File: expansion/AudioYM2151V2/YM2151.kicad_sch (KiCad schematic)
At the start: 17 parts, among them U3 LTC6903, U4 YM2151, U5 YM3012, U6 TL064

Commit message: more work on new audio card
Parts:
- added C48, C49: 4.7uF, symbol Device:C_Polarized
- added R13, R14: 3K9, symbol Device:R
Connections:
- net YM_AUDIO_L: now also R13.2; no longer U6.1, U6.2 (-)
- net YM_AUDIO_R: now also R14.2; no longer U6.6 (-), U6.7
- new net: C48.1, U6.1, U6.2 (-)
- new net: C49.1, U6.6 (-), U6.7
- new net: C49.2, R14.1
- new net: C48.2, R13.1
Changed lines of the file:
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@@
   (junction (at 83.82 68.58) (diameter 0) (color 0 0 0 0)
   )
+  (junction (at 92.71 179.07) (diameter 0) (color 0 0 0 0)
+  )
+  (junction (at 246.38 127) (diameter 0) (color 0 0 0 0)
+  )
+  (junction (at 92.71 166.37) (diameter 0) (color 0 0 0 0)
+  )
+  (junction (at 135.89 179.07) (diameter 0) (color 0 0 0 0)
+  )
+  (junction (at 246.38 144.78) (diameter 0) (color 0 0 0 0)
+  )
+  (junction (at 90.17 123.19) (diameter 0) (color 0 0 0 0)
+  )
+  (junction (at 124.46 119.38) (diameter 0) (color 0 0 0 0)
+  )
+  (junction (at 121.92 113.03) (diameter 0) (color 0 0 0 0)
+  )
+  (junction (at 207.01 31.75) (diameter 0) (color 0 0 0 0)
+  )
+  (junction (at 170.18 143.51) (diameter 0) (color 0 0 0 0)
+  )
+  (junction (at 179.07 41.91) (diameter 0) (color 0 0 0 0)
+  )
+  (junction (at 135.89 166.37) (diameter 0) (color 0 0 0 0)
+  )
+  (junction (at 127 121.92) (diameter 0) (color 0 0 0 0)
+  )
+  (junction (at 204.47 115.57) (diameter 0) (color 0 0 0 0)
+  )
+  (junction (at 207.01 64.77) (diameter 0) (color 0 0 0 0)
+  )
+  (junction (at 156.21 44.45) (diameter 0) (color 0 0 0 0)
+  )
+  (junction (at 146.05 39.37) (diameter 0) (color 0 0 0 0)
+  )
+  (junction (at 232.41 34.29) (diameter 0) (color 0 0 0 0)
+  )
+  (junction (at 129.54 107.95) (diameter 0) (color 0 0 0 0)
+  )
+  (junction (at 69.85 147.32) (diameter 0) (color 0 0 0 0)
+  )
   (junction (at 232.41 67.31) (diameter 0) (color 0 0 0 0)
-  )
-  (junction (at 92.71 179.07) (diameter 0) (color 0 0 0 0)
-  )
-  (junction (at 232.41 34.29) (diameter 0) (color 0 0 0 0)
-  )
-  (junction (at 246.38 127) (diameter 0) (color 0 0 0 0)
-  )
-  (junction (at 92.71 166.37) (diameter 0) (color 0 0 0 0)
-  )
-  (junction (at 135.89 179.07) (diameter 0) (color 0 0 0 0)
-  )
-  (junction (at 246.38 144.78) (diameter 0) (color 0 0 0 0)
-  )
-  (junction (at 90.17 123.19) (diameter 0) (color 0 0 0 0)
-  )
-  (junction (at 124.46 119.38) (diameter 0) (color 0 0 0 0)
-  )
-  (junction (at 121.92 113.03) (diameter 0) (color 0 0 0 0)
-  )
-  (junction (at 207.01 31.75) (diameter 0) (color 0 0 0 0)
-  )
-  (junction (at 170.18 143.51) (diameter 0) (color 0 0 0 0)
-  )
-  (junction (at 179.07 41.91) (diameter 0) (color 0 0 0 0)
-  )
-  (junction (at 135.89 166.37) (diameter 0) (color 0 0 0 0)
-  )
-  (junction (at 127 121.92) (diameter 0) (color 0 0 0 0)
-  )
-  (junction (at 204.47 115.57) (diameter 0) (color 0 0 0 0)
-  )
-  (junction (at 207.01 64.77) (diameter 0) (color 0 0 0 0)
-  )
-  (junction (at 156.21 44.45) (diameter 0) (color 0 0 0 0)
-  )
-  (junction (at 146.05 39.37) (diameter 0) (color 0 0 0 0)
-  )
-  (junction (at 129.54 107.95) (diameter 0) (color 0 0 0 0)
-  )
-  (junction (at 69.85 147.32) (diameter 0) (color 0 0 0 0)
   )
   (no_connect (at 80.01 63.5))
@@
     (stroke (width 0) (type default))
   )
-  (wire (pts (xy 232.41 34.29) (xy 242.57 34.29))
-    (stroke (width 0) (type default))
-  )
   (wire (pts (xy 191.77 110.49) (xy 207.01 110.49))
     (stroke (width 0) (type default))
@@
     (stroke (width 0) (type default))
   )
+  (wire (pts (xy 245.745 67.31) (xy 249.555 67.31))
+    (stroke (width 0) (type default))
+  )
+  (wire (pts (xy 232.41 67.31) (xy 238.125 67.31))
+    (stroke (width 0) (type default))
+  )
   (wire (pts (xy 123.19 179.07) (xy 135.89 179.07))
     (stroke (width 0) (type default))
@@
     (stroke (width 0) (type default))
   )
+  (wire (pts (xy 257.175 67.31) (xy 262.255 67.31))
+    (stroke (width 0) (type default))
+  )
   (wire (pts (xy 168.91 142.24) (xy 168.91 143.51))
     (stroke (width 0) (type default))
@@
     (stroke (width 0) (type default))
   )
+  (wire (pts (xy 245.745 34.29) (xy 249.555 34.29))
+    (stroke (width 0) (type default))
+  )
   (bus (pts (xy 43.18 125.73) (xy 43.18 128.27))
     (stroke (width 0) (type default))
@@
     (stroke (width 0) (type default))
   )
-  (wire (pts (xy 232.41 67.31) (xy 242.57 67.31))
-    (stroke (width 0) (type default))
-  )
   (wire (pts (xy 204.47 120.65) (xy 224.79 120.65))
     (stroke (width 0) (type default))
@@
   )
   (wire (pts (xy 69.85 96.52) (xy 69.85 99.06))
+    (stroke (width 0) (type default))
+  )
+  (wire (pts (xy 257.175 34.29) (xy 262.255 34.29))
+    (stroke (width 0) (type default))
+  )
+  (wire (pts (xy 232.41 34.29) (xy 238.125 34.29))
     (stroke (width 0) (type default))
   )
@@
     (effects (font (size 1.27 1.27)) (justify right))
   )
-  (hierarchical_label "YM_AUDIO_R" (shape output) (at 242.57 67.31 0) (fields_autoplaced)
+  (hierarchical_label "YM_AUDIO_R" (shape output) (at 262.255 67.31 0) (fields_autoplaced)
     (effects (font (size 1.27 1.27)) (justify left))
   )
-  (hierarchical_label "YM_AUDIO_L" (shape output) (at 242.57 34.29 0) (fields_autoplaced)
+  (hierarchical_label "YM_AUDIO_L" (shape output) (at 262.255 34.29 0) (fields_autoplaced)
     (effects (font (size 1.27 1.27)) (justify left))
   )
@@
         )
       )
+    )
+  )
+  (symbol (lib_id "Device:R") (at 253.365 67.31 90) (unit 1)
+    (in_bom yes) (on_board yes) (dnp no) (fields_autoplaced)
+    (property "Reference" "R14" (at 253.365 60.96 90)
+      (effects (font (size 1.27 1.27)))
+    )
+    (property "Value" "3K9" (at 253.365 63.5 90)
+      (effects (font (size 1.27 1.27)))
+    )
+    (property "Footprint" "" (at 253.365 69.088 90)
+      (effects (font (size 1.27 1.27)) hide)
+    )
+    (property "Datasheet" "~" (at 253.365 67.31 0)
+      (effects (font (size 1.27 1.27)) hide)
+    )
+    (pin "1")
+    (pin "2")
+    (instances
+      (project "AudioYM2151V2"
+        (path "/1a0b0354-7e8a-4de9-938d-3a3db9fe7fba/00000000-0000-0000-0000-000060b0be0a"
+          (reference "R14") (unit 1)
+        )
+      )
+    )
+  )
+  (symbol (lib_id "Device:C_Polarized") (at 241.935 34.29 90) (unit 1)
+    (in_bom yes) (on_board yes) (dnp no) (fields_autoplaced)
+    (property "Reference" "C48" (at 241.046 26.67 90)
+      (effects (font (size 1.27 1.27)))
+    )
+    (property "Value" "4.7uF" (at 241.046 29.21 90)
+      (effects (font (size 1.27 1.27)))
+    )
+    (property "Footprint" "" (at 245.745 33.3248 0)
+      (effects (font (size 1.27 1.27)) hide)
+    )
+    (property "Datasheet" "~" (at 241.935 34.29 0)
+      (effects (font (size 1.27 1.27)) hide)
+    )
+    (pin "2")
+    (pin "1")
+    (instances
+      (project "AudioYM2151V2"
+        (path "/1a0b0354-7e8a-4de9-938d-3a3db9fe7fba/00000000-0000-0000-0000-000060b0be0a"
+          (reference "C48") (unit 1)
+        )
+      )
+    )
+  )
+  (symbol (lib_id "Device:C_Polarized") (at 241.935 67.31 90) (unit 1)
+    (in_bom yes) (on_board yes) (dnp no) (fields_autoplaced)
+    (property "Reference" "C49" (at 241.046 59.69 90)
+      (effects (font (size 1.27 1.27)))
+    )
+    (property "Value" "4.7uF" (at 241.046 62.23 90)
+      (effects (font (size 1.27 1.27)))
+    )
+    (property "Footprint" "" (at 245.745 66.3448 0)
+      (effects (font (size 1.27 1.27)) hide)
+    )
+    (property "Datasheet" "~" (at 241.935 67.31 0)
+      (effects (font (size 1.27 1.27)) hide)
+    )
+    (pin "2")
+    (pin "1")
+    (instances
+      (project "AudioYM2151V2"
+        (path "/1a0b0354-7e8a-4de9-938d-3a3db9fe7fba/00000000-0000-0000-0000-000060b0be0a"
+          (reference "C49") (unit 1)
+        )
+      )
+    )
+  )
+  (symbol (lib_id "Device:R") (at 253.365 34.29 90) (unit 1)
+    (in_bom yes) (on_board yes) (dnp no) (fields_autoplaced)
+    (property "Reference" "R13" (at 253.365 27.94 90)
+      (effects (font (size 1.27 1.27)))
+    )
+    (property "Value" "3K9" (at 253.365 30.48 90)
+      (effects (font (size 1.27 1.27)))
+    )
+    (property "Footprint" "" (at 253.365 36.068 90)
+      (effects (font (size 1.27 1.27)) hide)
+    )
+    (property "Datasheet" "~" (at 253.365 34.29 0)
+      (effects (font (size 1.27 1.27)) hide)
+    )
+    (pin "1")
+    (pin "2")
+    (instances
+      (project "AudioYM2151V2"
+        (path "/1a0b0354-7e8a-4de9-938d-3a3db9fe7fba/00000000-0000-0000-0000-000060b0be0a"
+          (reference "R13") (unit 1)
+        )
+      )

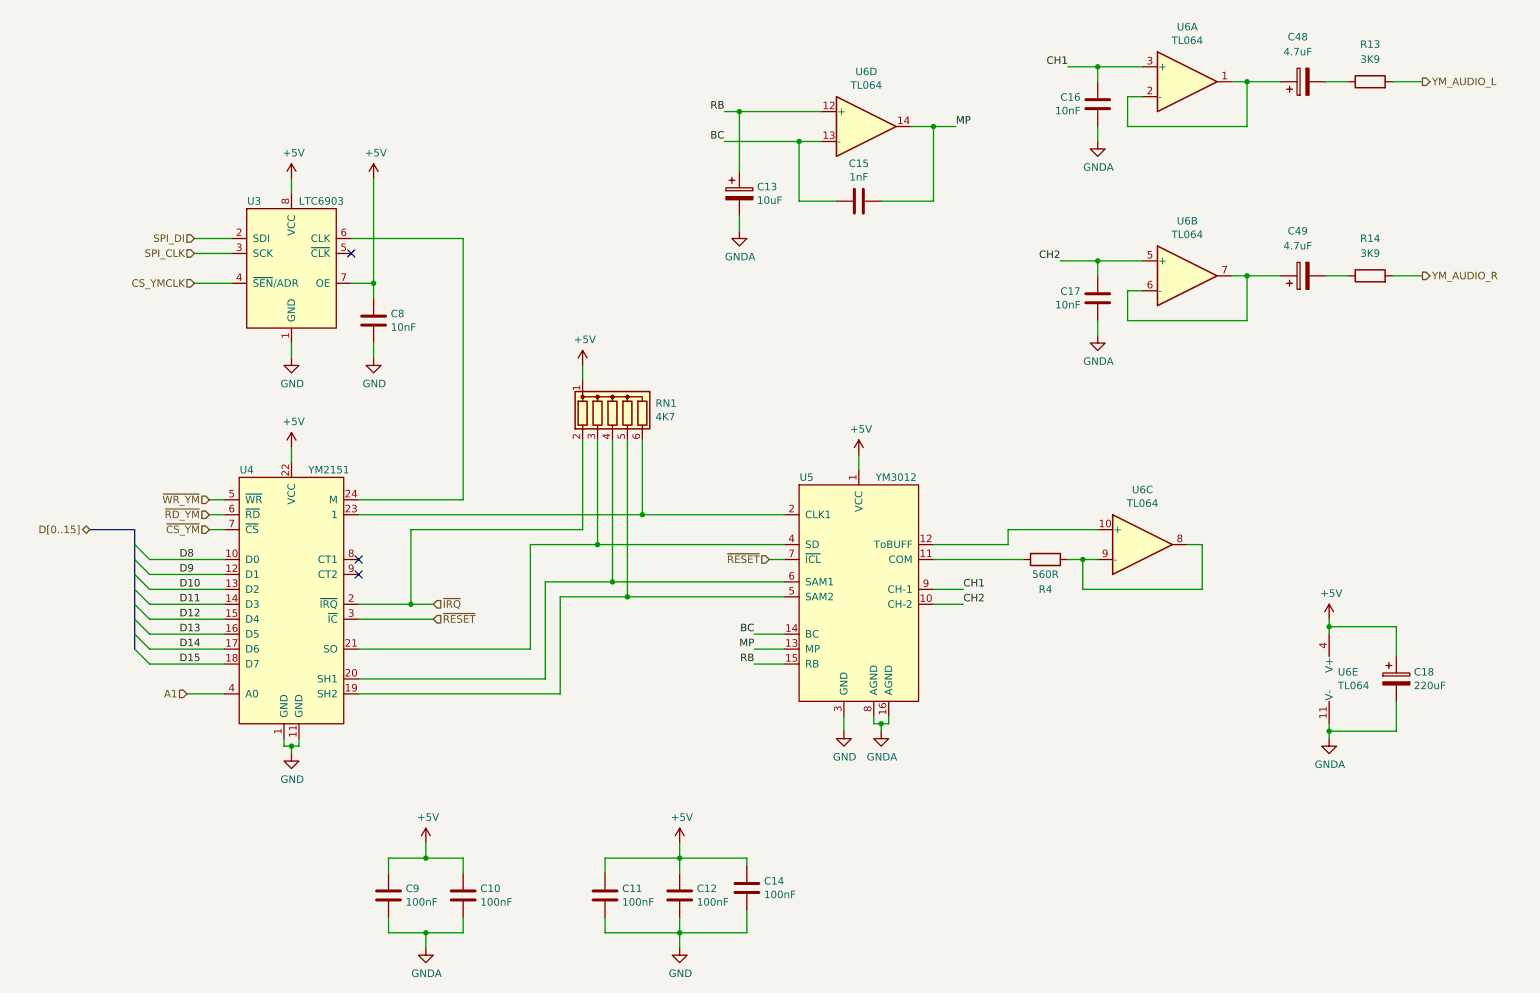
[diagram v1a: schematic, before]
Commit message: Updated YM2151 Board
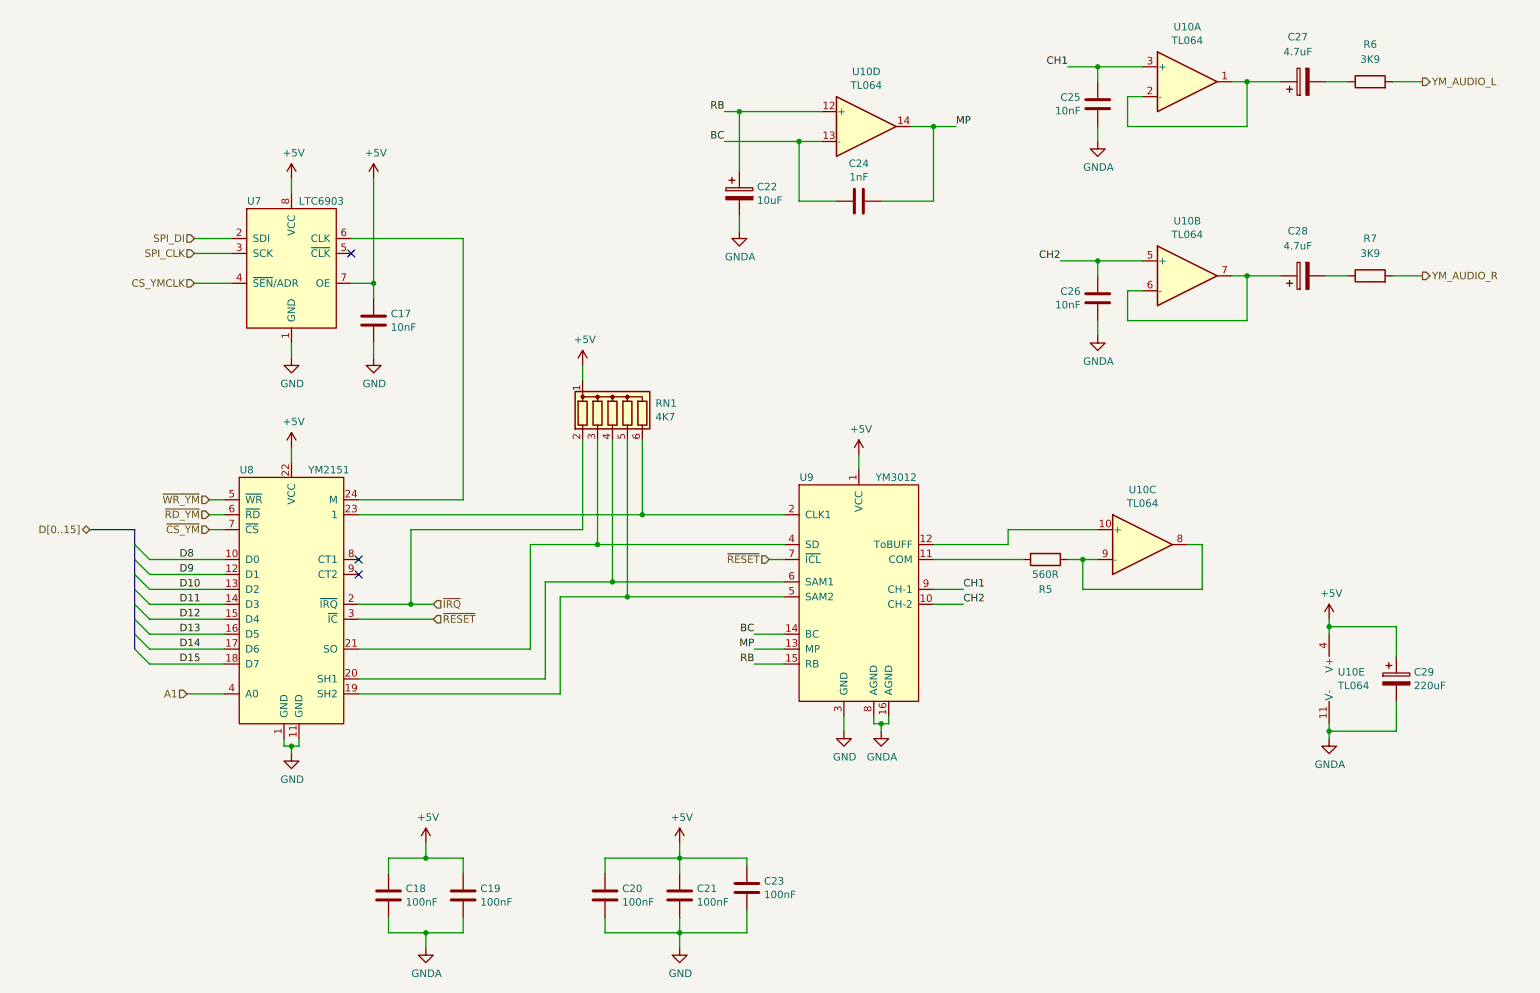
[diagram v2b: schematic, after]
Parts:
- C27: renamed from C48; footprint (none) -> Capacitor_THT:CP_Radial_D10.0mm_P5.00mm
- C28: renamed from C49; footprint (none) -> Capacitor_THT:CP_Radial_D10.0mm_P5.00mm
- R6: renamed from R13; footprint (none) -> Resistor_THT:R_Axial_DIN0207_L6.3mm_D2.5mm_P10.16mm_Horizontal
- R7: renamed from R14; footprint (none) -> Resistor_THT:R_Axial_DIN0207_L6.3mm_D2.5mm_P10.16mm_Horizontal
- U10: renamed from U6; footprint Package_DIP:DIP-14_W7.62mm_Socket -> Package_DIP:DIP-8_W7.62mm_Socket
- renumbered C8 to C17, C9 to C18, C10 to C19, C11 to C20, C12 to C21, C13 to C22, C14 to C23, C15 to C24, C16 to C25, C17 to C26, C18 to C29, R4 to R5, U3 to U7, U4 to U8, U5 to U9

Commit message: More changes to YM2151V2
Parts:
- renumbered C23 to C10, C24 to C11, C25 to C12, C26 to C13, C27 to C14, C28 to C15, C29 to C16, C17 to C4, C18 to C5, C19 to C6, C20 to C7, C21 to C8, C22 to C9, R5 to R3, R6 to R4, R7 to R5, U7 to U3, U8 to U4, U9 to U5, U10 to U6
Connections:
- net D10 renamed D2
- net D11 renamed D3
- net D12 renamed D4
- net D13 renamed D5
- net D14 renamed D6
- net D15 renamed D7
- net D8 renamed D0
- net D9 renamed D1

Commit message: Completed YM2151V2 schematic
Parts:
- U3: renamed from U4; footprint Package_DIP:DIP-24_W15.24mm_Socket -> Package_DIP:DIP-24_W15.24mm
- U5: renamed from U6; footprint Package_DIP:DIP-8_W7.62mm_Socket -> Package_DIP:DIP-14_W7.62mm_Socket
- renumbered R3 to R4, R4 to R5, R5 to R6, U3 to U2, U5 to U4
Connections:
- net A1 renamed A0

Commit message: Starting pcb layout
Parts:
- C14, C15: footprint Capacitor_THT:CP_Radial_D10.0mm_P5.00mm -> Capacitor_THT:CP_Radial_D5.0mm_P2.50mm
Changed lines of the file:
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@@
       (effects (font (size 1.27 1.27)))
     )
-    (property "Footprint" "Capacitor_THT:CP_Radial_D10.0mm_P5.00mm" (at 245.745 33.3248 0)
+    (property "Footprint" "Capacitor_THT:CP_Radial_D5.0mm_P2.50mm" (at 245.745 33.3248 0)
       (effects (font (size 1.27 1.27)) hide)
     )
@@
       (effects (font (size 1.27 1.27)))
     )
-    (property "Footprint" "Capacitor_THT:CP_Radial_D10.0mm_P5.00mm" (at 245.745 66.3448 0)
+    (property "Footprint" "Capacitor_THT:CP_Radial_D5.0mm_P2.50mm" (at 245.745 66.3448 0)
       (effects (font (size 1.27 1.27)) hide)
     )
